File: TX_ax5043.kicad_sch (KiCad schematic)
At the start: 31 parts, among them J7 2118714-2, P6 CONUFL001-SMD-T, P7 CONUFL001-SMD-T, Q7 DMP2037U, U23 AX5043

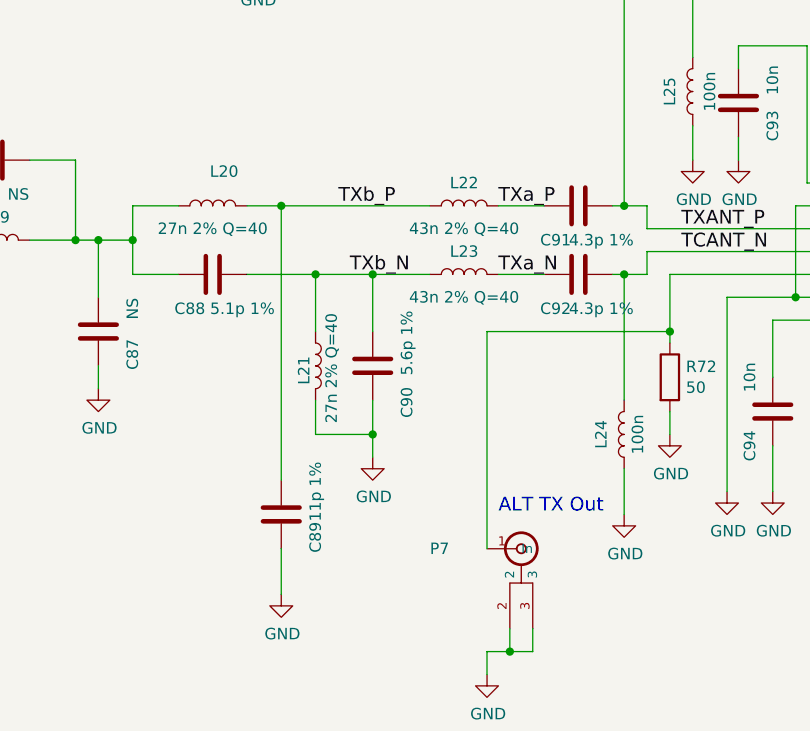
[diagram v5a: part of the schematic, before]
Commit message: More 0402 updates and cleanups
Signed-off-by: Corey Minyard <corey@minyard.net>
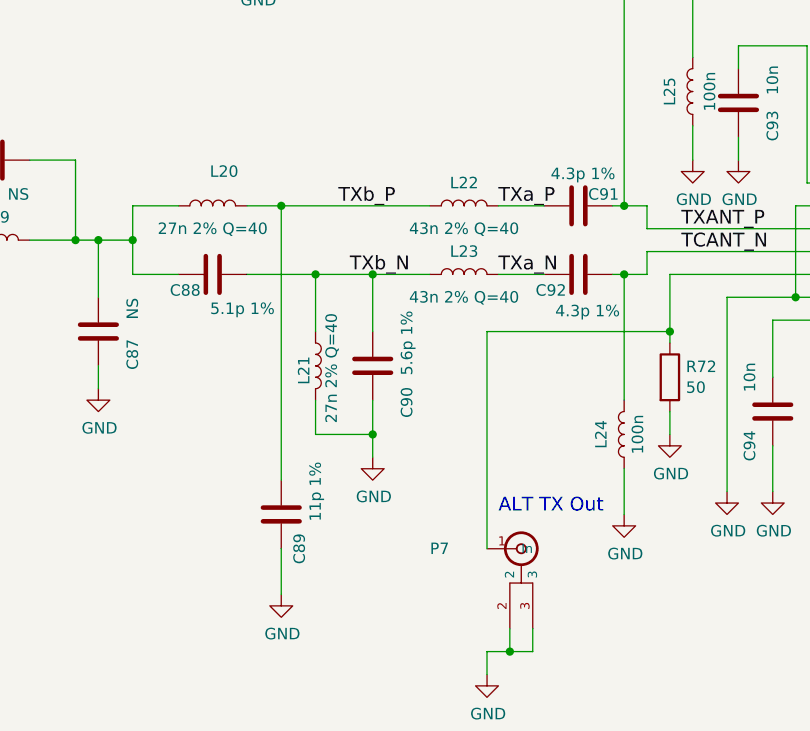
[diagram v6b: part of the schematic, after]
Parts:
- C85, C86, C87, C88, C89, C90, C91, C92, C93, C94, C95, C96, C97: footprint Capacitor_SMD:C_0603_1608Metric_Pad1.08x0.95mm_HandSolder -> Capacitor_SMD:C_0402_1005Metric_Pad0.74x0.62mm_HandSolder
- R72, R73, R74, R75: footprint Resistor_SMD:R_0603_1608Metric_Pad0.98x0.95mm_HandSolder -> Resistor_SMD:R_0402_1005Metric_Pad0.72x0.64mm_HandSolder
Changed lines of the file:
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@@
 		(dnp no)
 		(property "Reference" "C91"
-			(at 210.82 135.89 90)
+			(at 216.154 130.81 90)
 			(effects
 				(font
@@
 		)
 		(property "Value" "4.3p 1%"
-			(at 215.9 135.89 90)
-			(effects
-				(font
-					(size 1.27 1.27)
-				)
-			)
-		)
-		(property "Footprint" "Capacitor_SMD:C_0603_1608Metric_Pad1.08x0.95mm_HandSolder"
+			(at 213.868 128.524 90)
+			(effects
+				(font
+					(size 1.27 1.27)
+				)
+			)
+		)
+		(property "Footprint" "Capacitor_SMD:C_0402_1005Metric_Pad0.74x0.62mm_HandSolder"
 			(at 209.55 133.0452 0)
 			(effects
@@
 		(dnp no)
 		(property "Reference" "C92"
-			(at 210.82 143.51 90)
+			(at 210.312 141.478 90)
 			(effects
 				(font
@@
 		)
 		(property "Value" "4.3p 1%"
-			(at 215.9 143.51 90)
-			(effects
-				(font
-					(size 1.27 1.27)
-				)
-			)
-		)
-		(property "Footprint" "Capacitor_SMD:C_0603_1608Metric_Pad1.08x0.95mm_HandSolder"
+			(at 214.376 143.764 90)
+			(effects
+				(font
+					(size 1.27 1.27)
+				)
+			)
+		)
+		(property "Footprint" "Capacitor_SMD:C_0402_1005Metric_Pad0.74x0.62mm_HandSolder"
 			(at 209.55 140.6652 0)
 			(effects
@@
 			)
 		)
-		(property "Footprint" "Capacitor_SMD:C_0603_1608Metric_Pad1.08x0.95mm_HandSolder"
+		(property "Footprint" "Capacitor_SMD:C_0402_1005Metric_Pad0.74x0.62mm_HandSolder"
 			(at 232.1052 124.46 0)
 			(effects
@@
 			)
 		)
-		(property "Footprint" "Capacitor_SMD:C_0603_1608Metric_Pad1.08x0.95mm_HandSolder"
+		(property "Footprint" "Capacitor_SMD:C_0402_1005Metric_Pad0.74x0.62mm_HandSolder"
 			(at 290.5252 110.49 0)
 			(effects
@@
 			)
 		)
-		(property "Footprint" "Capacitor_SMD:C_0603_1608Metric_Pad1.08x0.95mm_HandSolder"
+		(property "Footprint" "Capacitor_SMD:C_0402_1005Metric_Pad0.74x0.62mm_HandSolder"
 			(at 191.4652 153.67 0)
 			(effects
@@
 		(dnp no)
 		(property "Reference" "C88"
-			(at 170.18 143.51 90)
+			(at 169.672 141.478 90)
 			(effects
 				(font
@@
 			)
 		)
-		(property "Footprint" "Capacitor_SMD:C_0603_1608Metric_Pad1.08x0.95mm_HandSolder"
+		(property "Footprint" "Capacitor_SMD:C_0402_1005Metric_Pad0.74x0.62mm_HandSolder"
 			(at 168.91 140.6652 0)
 			(effects
@@
 		(dnp no)
 		(property "Reference" "C89"
-			(at 184.15 168.91 90)
+			(at 182.372 170.18 90)
 			(effects
 				(font
@@
 			)
 		)
-		(property "Footprint" "Capacitor_SMD:C_0603_1608Metric_Pad1.08x0.95mm_HandSolder"
+		(property "Footprint" "Capacitor_SMD:C_0402_1005Metric_Pad0.74x0.62mm_HandSolder"
 			(at 181.3052 170.18 0)
 			(effects
@@
 			)
 		)
-		(property "Footprint" "Capacitor_SMD:C_0603_1608Metric_Pad1.08x0.95mm_HandSolder"
+		(property "Footprint" "Capacitor_SMD:C_0402_1005Metric_Pad0.74x0.62mm_HandSolder"
 			(at 144.78 127.9652 0)
 			(effects
@@
 			)
 		)
-		(property "Footprint" "Capacitor_SMD:C_0603_1608Metric_Pad1.08x0.95mm_HandSolder"
+		(property "Footprint" "Capacitor_SMD:C_0402_1005Metric_Pad0.74x0.62mm_HandSolder"
 			(at 141.9352 149.86 0)
 			(effects
@@
 			)
 		)
-		(property "Footprint" "Capacitor_SMD:C_0603_1608Metric_Pad1.08x0.95mm_HandSolder"
+		(property "Footprint" "Capacitor_SMD:C_0402_1005Metric_Pad0.74x0.62mm_HandSolder"
 			(at 160.9852 149.86 0)
 			(effects
@@
 			)
 		)
-		(property "Footprint" "Capacitor_SMD:C_0603_1608Metric_Pad1.08x0.95mm_HandSolder"
+		(property "Footprint" "Capacitor_SMD:C_0402_1005Metric_Pad0.74x0.62mm_HandSolder"
 			(at 235.9152 158.75 0)
 			(effects
@@
 			)
 		)
-		(property "Footprint" "Resistor_SMD:R_0603_1608Metric_Pad0.98x0.95mm_HandSolder"
+		(property "Footprint" "Resistor_SMD:R_0402_1005Metric_Pad0.72x0.64mm_HandSolder"
 			(at 270.002 81.28 90)
 			(effects
@@
 			)
 		)
-		(property "Footprint" "Resistor_SMD:R_0603_1608Metric_Pad0.98x0.95mm_HandSolder"
+		(property "Footprint" "Resistor_SMD:R_0402_1005Metric_Pad0.72x0.64mm_HandSolder"
 			(at 278.892 81.28 90)
 			(effects
@@
 			)
 		)
-		(property "Footprint" "Resistor_SMD:R_0603_1608Metric_Pad0.98x0.95mm_HandSolder"
+		(property "Footprint" "Resistor_SMD:R_0402_1005Metric_Pad0.72x0.64mm_HandSolder"
 			(at 221.742 151.13 90)
 			(effects
@@
 			)
 		)
-		(property "Footprint" "Capacitor_SMD:C_0603_1608Metric_Pad1.08x0.95mm_HandSolder"
+		(property "Footprint" "Capacitor_SMD:C_0402_1005Metric_Pad0.74x0.62mm_HandSolder"
 			(at 258.7752 99.06 0)
 			(effects
@@
 			)
 		)
-		(property "Footprint" "Resistor_SMD:R_0603_1608Metric_Pad0.98x0.95mm_HandSolder"
+		(property "Footprint" "Resistor_SMD:R_0402_1005Metric_Pad0.72x0.64mm_HandSolder"
 			(at 300.99 146.558 90)
 			(effects
@@
 			)
 		)
-		(property "Footprint" "Capacitor_SMD:C_0603_1608Metric_Pad1.08x0.95mm_HandSolder"
+		(property "Footprint" "Capacitor_SMD:C_0402_1005Metric_Pad0.74x0.62mm_HandSolder"
 			(at 237.7948 87.63 0)
 			(effects

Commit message: Work on cleaning up all values for things
Signed-off-by: Corey Minyard <corey@minyard.net>
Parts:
- C85, C86, C87: now not fitted
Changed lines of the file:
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@@
 		(in_bom yes)
 		(on_board yes)
-		(dnp no)
+		(dnp yes)
 		(property "Reference" "C86"
 			(at 146.05 130.81 90)
@@
 		(in_bom yes)
 		(on_board yes)
-		(dnp no)
+		(dnp yes)
 		(property "Reference" "C85"
 			(at 144.78 148.59 90)
@@
 		(in_bom yes)
 		(on_board yes)
-		(dnp no)
+		(dnp yes)
 		(property "Reference" "C87"
 			(at 163.83 148.59 90)

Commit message: More work on components
Signed-off-by: Corey Minyard <corey@minyard.net>
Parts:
- C85, C86, C87: value NS -> ~
- FB8: value 1K @ 100MHz -> 1K@100MHz
- L20, L21: value 27n 2% Q=40 -> 27n 2% Q=82
- L22, L23: value 43n 2% Q=40 -> 43n 2% Q=82
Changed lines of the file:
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@@
 			)
 		)
-		(property "Value" "27n 2% Q=40"
+		(property "Value" "27n 2% Q=82"
 			(at 185.928 150.114 90)
 			(effects
@@
 			)
 		)
-		(property "Value" "NS"
-			(at 151.13 130.81 90)
+		(property "Value" "~"
+			(at 148.59 127 90)
 			(effects
 				(font
@@
 			)
 		)
-		(property "Value" "NS"
+		(property "Value" "~"
 			(at 144.78 143.51 90)
 			(effects
@@
 			)
 		)
-		(property "Value" "NS"
+		(property "Value" "~"
 			(at 163.83 143.51 90)
 			(effects
@@
 			)
 		)
-		(property "Value" "1K @ 100MHz"
+		(property "Value" "1K@100MHz"
 			(at 303.4919 77.47 90)
 			(effects
@@
 			)
 		)
-		(property "Value" "43n 2% Q=40"
+		(property "Value" "43n 2% Q=82"
 			(at 200.66 142.24 90)
 			(effects
@@
 			)
 		)
-		(property "Value" "43n 2% Q=40"
+		(property "Value" "43n 2% Q=82"
 			(at 200.66 134.62 90)
 			(effects
@@
 			)
 		)
-		(property "Value" "27n 2% Q=40"
+		(property "Value" "27n 2% Q=82"
 			(at 172.72 134.62 90)
 			(effects
